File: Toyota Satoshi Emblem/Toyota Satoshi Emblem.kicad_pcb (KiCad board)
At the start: 2 copper layers, 175 x 100 mm, 337 parts

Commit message: v1.7
More changes to LED pcb. Realized I could link ambers in 3 link series and removing 6 resistors per letter (less heat). Have to redo everything again
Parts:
- removed the R2 at (70.2, 68.6)
- added REF**: Pad 1, afootprints:Pad 1, F.Cu at (81.6, 60.0)
- added REF**: Pad 1, afootprints:Pad 1, F.Cu at (73.7, 60.0)
- added REF**: Pad 1, afootprints:Pad 1, F.Cu at (89.5, 87.8)
- added REF**: Pad 1, afootprints:Pad 1, F.Cu at (97.5, 87.8)
- added REF**: Pad 1, afootprints:Pad 1, F.Cu at (77.6, 60.0)
- added REF**: Pad 1, afootprints:Pad 1, F.Cu at (93.5, 87.8)
- moved R36 187.8 mm to (99.8, 83.2), turned to 180 degrees
- moved R25 184.5 mm to (108.5, 92.8)
- moved R30 179.0 mm to (105.2, 86.0), turned to 180 degrees
- moved R27 176.3 mm to (100.2, 134.2), turned to 180 degrees
- moved R19 172.0 mm to (111.0, 99.0)
- moved R32 170.7 mm to (117.8, 114.2)
- moved D138 168.9 mm to (99.1, 316.7)
- moved R26 165.2 mm to (113.3, 114.2)
- moved R35 164.5 mm to (76.2, 100.4), turned to -90 degrees
- moved D25 164.4 mm to (107.8, 90.0)
- moved R33 162.4 mm to (96.5, 134.1), turned to 90 degrees
- moved R22 160.7 mm to (71.0, 120.5), turned to 90 degrees
- moved R23 152.6 mm to (80.5, 94.2), turned to 180 degrees
- moved R31 141.4 mm to (113.2, 92.5)
- moved R20 138.6 mm to (116.5, 120.8), turned to 180 degrees
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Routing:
- net Net-(D43-Pad1): track 0.00 -> 210.7 mm
- net Net-(J2-Pad2): track 0.00 -> 189.9 mm
- net Net-(D25-Pad1): track 0.00 -> 141.8 mm
- net Net-(D1-Pad1): track 151.3 -> 215.5 mm
- net Net-(D28-Pad2): track 0.00 -> 34.2 mm
- net Net-(D42-Pad1): track 0.00 -> 29.1 mm
- net Net-(D41-Pad1): track 0.00 -> 19.1 mm
- net Net-(D26-Pad2): track 0.00 -> 18.2 mm
- net Net-(D27-Pad2): track 0.00 -> 16.3 mm
- net Net-(D25-Pad2): track 0.00 -> 16.1 mm
- net Net-(D39-Pad1): track 0.00 -> 15.7 mm
- net Net-(D40-Pad1): track 0.00 -> 15.1 mm
- net Net-(R28-Pad2): track 0.00 -> 13.8 mm
- net Net-(D37-Pad1): track 0.00 -> 13.6 mm
- net Net-(D29-Pad2): track 0.00 -> 12.8 mm
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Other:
- outline, holes or cut-outs redrawn
- board text added: "7V"
- board text added: "amber"
- board text added: "dhoefer"
- board text added: "white"

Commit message: v1.8
Letter T is now complete
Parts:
- removed D100, D101, D102, D103, D104, D105, D106, D107, D108, D121, D122, D123, D124, D125, D126, D127, D128, D129, D130, D131, D132, D145, D146, D147, D148, D149, D150, D151, D152, D153, D154, D155, D156, D157, D158, D159, D160, D161, D162, D163, D164, D165, D166, D167, D168, D31, D32, D33, D34, D35, D36, D49, D50, D51, D52, D53, D54, D55, D56, D57, D58, D59, D60, D73, D74, D75, D76, D77, D78, D79, D80, D81, D82, D83, D84, D97, D98, D99: W_LED, afootprints:5730 LED W
- removed D109, D110, D111, D112, D113, D114, D115, D116, D117, D118, D119, D120, D133, D134, D135, D136, D137, D138, D139, D140, D141, D142, D143, D144, D169, D170, D171, D172, D173, D174, D175, D176, D177, D178, D179, D180, D181, D182, D183, D184, D185, D186, D187, D188, D189, D190, D191, D192, D37, D38, D39, D40, D41, D42, D43, D44, D45, D46, D47, D48, D61, D62, D63, D64, D65, D66, D67, D68, D69, D70, D71, D72, D85, D86, D87, D88, D89, D90, D91, D92, D93, D94, D95, D96: A_LED, afootprints:5730 LED A
- removed R100, R101, R102, R103, R104, R105, R106, R107, R108, R121, R122, R123, R124, R125, R126, R127, R128, R129, R13, R130, R131, R132, R133, R134, R135, R136, R137, R138, R139, R14, R140, R141, R142, R143, R144, R15, R16, R17, R18, R25, R26, R27, R28, R29, R30, R31, R32, R33, R34, R35, R36, R43, R44, R45, R46, R47, R48, R49, R50, R51, R52, R53, R54, R61, R62, R63, R64, R65, R66, R67, R68, R69, R70, R71, R72, R79, R80, R81, R82, R83, R84, R85, R86, R87, R88, R89, R90, R97, R98, R99: 8.2, afootprints:1206 R
- removed R109, R110, R111, R112, R113, R114, R115, R116, R117, R118, R119, R120, R19, R20, R21, R22, R23, R24, R37, R38, R39, R40, R41, R42, R55, R56, R57, R58, R59, R60, R73, R74, R75, R76, R77, R78, R91, R92, R93, R94, R95, R96: 3.3, afootprints:1206 R
- removed the REF** at (89.5, 87.8)
- removed the REF** at (97.5, 87.8)
- removed the REF** at (93.5, 87.8)
- D1, D10, D11, D12, D2, D3, D4, D5, D6, D7, D8, D9: value W_LED -> WLED
- D13, D14, D15, D16, D17, D18, D19, D20, D21, D22, D23, D24: value A_LED -> ALED
- D25, D26, D27, D28, D29, D30: value W_LED -> ALED; footprint afootprints:5730 LED W -> afootprints:5730 LED A
- R1, R2, R4, R5, R6: value 3.3 -> 4.7
- R10, R11, R12, R7, R8, R9: value 8.2 -> 4.7
- R3: value 3.3 -> 4,7
- moved D28 70.0 mm to (102.4, 62.5), turned to -90 degrees
- moved D27 66.7 mm to (89.8, 64.9)
- moved D29 53.9 mm to (89.8, 55.1), turned to 0 degrees
- moved D26 52.4 mm to (97.1, 61.8)
- moved D24 45.8 mm to (56.2, 69.0), turned to -90 degrees
- moved D25 33.2 mm to (97.1, 58.6), turned to 180 degrees
- moved D5 32.7 mm to (67.6, 55.4)
- moved D6 32.6 mm to (60.8, 48.4), turned to 90 degrees
- moved D9 31.9 mm to (82.4, 55.4)
- moved D30 31.4 mm to (75.0, 55.4), turned to 0 degrees
- moved D10 31.2 mm to (97.5, 55.5)
- moved D23 31.1 mm to (60.0, 64.6), turned to 90 degrees
- moved D17 30.9 mm to (52.8, 44.0), turned to 90 degrees
- moved D18 28.2 mm to (54.8, 56.6)
- moved D12 26.5 mm to (97.1, 64.9), turned to 0 degrees
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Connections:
- D11 pad 1: Net-(D11-Pad1) -> Net-(D1-Pad1)
- D12 pad 1: Net-(D12-Pad1) -> Net-(D11-Pad2)
- D14 pad 2: Net-(D14-Pad2) -> Net-(D13-Pad1)
- D15 pad 2: Net-(D15-Pad2) -> Net-(D14-Pad1)
- D17 pad 2: Net-(D17-Pad2) -> Net-(D16-Pad1)
- D18 pad 1: Net-(D18-Pad1) -> Net-(D15-Pad1)
- D18 pad 2: Net-(D18-Pad2) -> Net-(D17-Pad1)
- D19 pad 2: Net-(D13-Pad1) -> Net-(D19-Pad2)
- D2 pad 1: Net-(D1-Pad1) -> Net-(D1-Pad2)
- D20 pad 1: Net-(D19-Pad1) -> Net-(D20-Pad1)
- D20 pad 2: Net-(D14-Pad1) -> Net-(D19-Pad1)
- D21 pad 1: Net-(D19-Pad1) -> Net-(D15-Pad1)
- D21 pad 2: Net-(D15-Pad1) -> Net-(D20-Pad1)
- D22 pad 1: Net-(D19-Pad1) -> Net-(D22-Pad1)
- D22 pad 2: Net-(D16-Pad1) -> Net-(D22-Pad2)
- D23 pad 1: Net-(D19-Pad1) -> Net-(D23-Pad1)
- D23 pad 2: Net-(D17-Pad1) -> Net-(D22-Pad1)
- D24 pad 1: Net-(D19-Pad1) -> Net-(D15-Pad1)
- D24 pad 2: Net-(D18-Pad1) -> Net-(D23-Pad1)
- D26 pad 1: Net-(D25-Pad1) -> Net-(D26-Pad1)
- D26 pad 2: Net-(D26-Pad2) -> Net-(D25-Pad1)
- D27 pad 1: Net-(D25-Pad1) -> Net-(D15-Pad1)
- D27 pad 2: Net-(D27-Pad2) -> Net-(D26-Pad1)
- D28 pad 1: Net-(D25-Pad1) -> Net-(D28-Pad1)
- D29 pad 1: Net-(D25-Pad1) -> Net-(D29-Pad1)
- D29 pad 2: Net-(D29-Pad2) -> Net-(D28-Pad1)
- D30 pad 1: Net-(D25-Pad1) -> Net-(D15-Pad1)
- D30 pad 2: Net-(D30-Pad2) -> Net-(D29-Pad1)
- D4 pad 1: Net-(D1-Pad1) -> Net-(D3-Pad2)
- D4 pad 2: Net-(D10-Pad1) -> Net-(D4-Pad2)
- D5 pad 2: Net-(D11-Pad1) -> Net-(D5-Pad2)
- D6 pad 1: Net-(D1-Pad1) -> Net-(D5-Pad2)
- D6 pad 2: Net-(D12-Pad1) -> Net-(D6-Pad2)
- D7 pad 1: Net-(D1-Pad2) -> Net-(D1-Pad1)
- D8 pad 1: Net-(D2-Pad2) -> Net-(D7-Pad2)
- D9 pad 1: Net-(D3-Pad2) -> Net-(D1-Pad1)
- D9 pad 2: Net-(D9-Pad2) -> Net-(D10-Pad1)
- R1 pad 2: Net-(D7-Pad2) -> Net-(D2-Pad2)
- R10 pad 2: Net-(R10-Pad2) -> Net-(D22-Pad2)
- R11 pad 2: Net-(R11-Pad2) -> Net-(D25-Pad2)
- R12 pad 2: Net-(R12-Pad2) -> Net-(D28-Pad2)
- R2 pad 2: Net-(D8-Pad2) -> Net-(D4-Pad2)
- R3 pad 2: Net-(D9-Pad2) -> Net-(D6-Pad2)
- R4 pad 2: Net-(D10-Pad2) -> Net-(D8-Pad2)
- R5 pad 2: Net-(D11-Pad2) -> Net-(D10-Pad2)
- R7 pad 2: Net-(R13-Pad1) -> Net-(D13-Pad2)
- R8 pad 2: Net-(R14-Pad1) -> Net-(D16-Pad2)
- R9 pad 2: Net-(R15-Pad1) -> Net-(D19-Pad2)
- REF** pad 1: Net-(D19-Pad1) -> Net-(D15-Pad1)
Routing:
- net Net-(D43-Pad1): track 210.7 -> 0.00 mm
- net Net-(J2-Pad2): track 189.9 -> 0.00 mm
- net Net-(D25-Pad1): track 141.8 -> 3.20 mm
- net Net-(D1-Pad1): track 215.5 -> 81.7 mm
- net Net-(D19-Pad1): track 139.0 -> 8.05 mm
- net Net-(D15-Pad1): track 11.3 -> 71.8 mm
- net Net-(D17-Pad2): track 31.9 -> 0.00 mm
- net Net-(D42-Pad1): track 29.1 -> 0.00 mm
- net Net-(D28-Pad2): track 34.2 -> 13.0 mm
- net Net-(D12-Pad2): track 31.6 -> 12.4 mm
- net Net-(D41-Pad1): track 19.1 -> 0.00 mm
- net Net-(D12-Pad1): track 19.0 -> 0.00 mm
- net Net-(D26-Pad2): track 18.2 -> 0.00 mm
- net Net-(D28-Pad1): track 0.00 -> 17.4 mm
- net Net-(D27-Pad2): track 16.3 -> 0.00 mm
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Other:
- board text added: "7.5V"
- board text added: "Daniel Hoefer"
- board text added: "Isaiah 60:1"
- board text added: "a"
- board text added: "w"
- board text removed: "7V"
- board text removed: "amber"
- board text removed: "dhoefer"
- board text removed: "white"

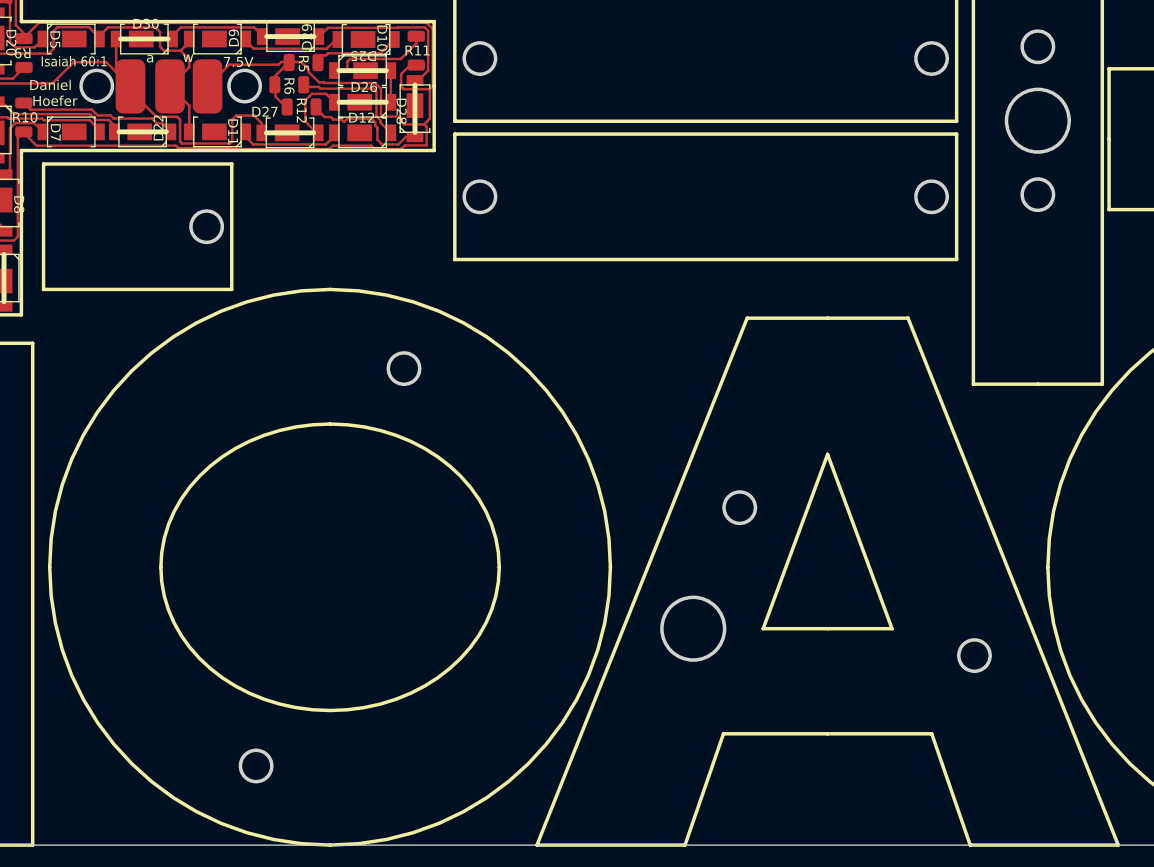
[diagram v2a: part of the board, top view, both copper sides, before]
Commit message: v1.9
Letter O and A are now complete
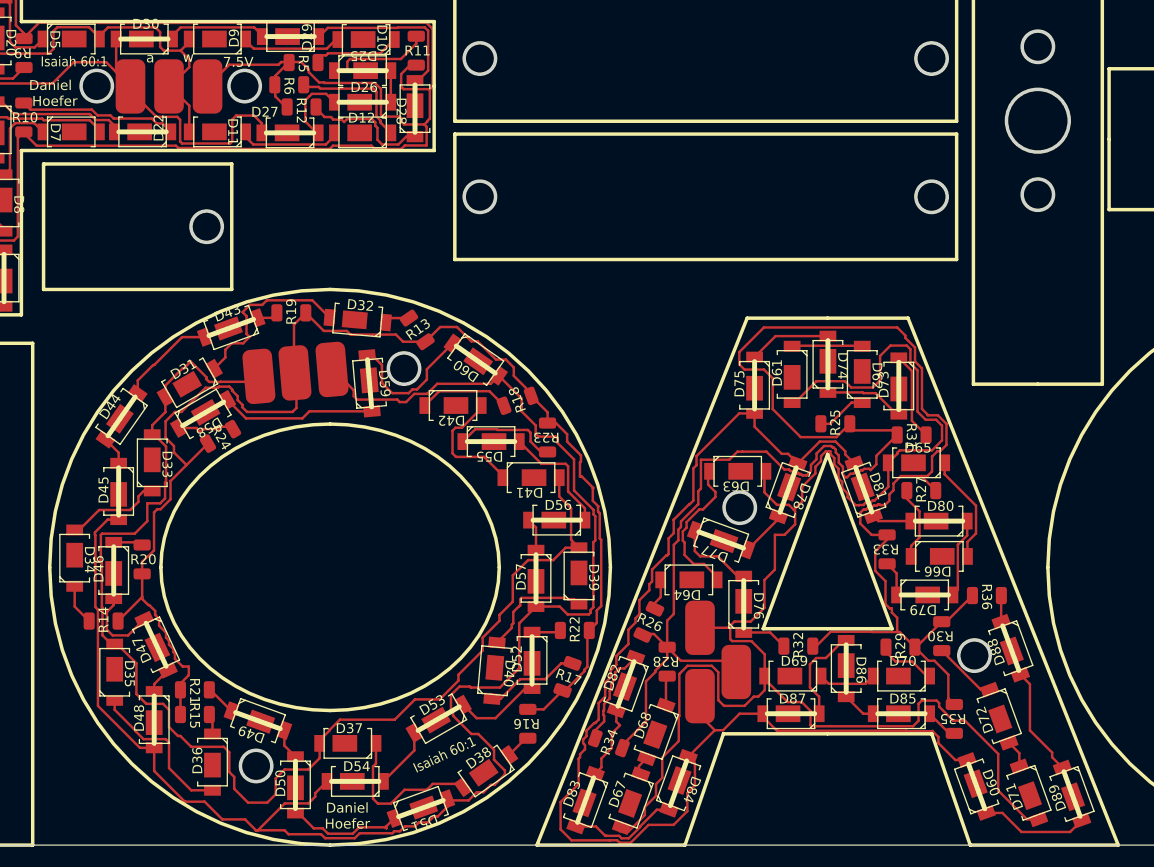
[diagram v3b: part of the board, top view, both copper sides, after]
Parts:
- added D31: WLED, afootprints:5730 LED W, F.Cu at (79.6, 90.2)
- added D32: WLED, afootprints:5730 LED W, F.Cu at (96.6, 83.8)
- added D33: WLED, afootprints:5730 LED W, F.Cu at (75.8, 98.3)
- added D34: WLED, afootprints:5730 LED W, F.Cu at (68.0, 108.0)
- added D35: WLED, afootprints:5730 LED W, F.Cu at (72.0, 119.5)
- added D36: WLED, afootprints:5730 LED W, F.Cu at (81.9, 128.6)
- added D37: WLED, afootprints:5730 LED W, F.Cu at (95.6, 126.7)
- added D38: WLED, afootprints:5730 LED W, F.Cu at (109.6, 129.5)
- added D39: WLED, afootprints:5730 LED W, F.Cu at (119.0, 109.8)
- added D40: WLED, afootprints:5730 LED W, F.Cu at (110.5, 119.3)
- added D41: WLED, afootprints:5730 LED W, F.Cu at (114.2, 99.8)
- added D42: WLED, afootprints:5730 LED W, F.Cu at (106.2, 92.5)
- added D43: ALED, afootprints:5730 LED A, F.Cu at (83.8, 84.6)
- added D44: ALED, afootprints:5730 LED A, F.Cu at (72.7, 93.6)
- added D45: ALED, afootprints:5730 LED A, F.Cu at (72.4, 101.2)
- added D46: ALED, afootprints:5730 LED A, F.Cu at (71.9, 109.2)
- added D47: ALED, afootprints:5730 LED A, F.Cu at (76.2, 116.7)
- added D48: ALED, afootprints:5730 LED A, F.Cu at (76.0, 124.3)
- added D49: ALED, afootprints:5730 LED A, F.Cu at (86.5, 124.4)
- added D50: ALED, afootprints:5730 LED A, F.Cu at (90.3, 130.9)
- added D51: ALED, afootprints:5730 LED A, F.Cu at (103.0, 133.3)
- added D52: ALED, afootprints:5730 LED A, F.Cu at (114.2, 118.3)
- added D53: ALED, afootprints:5730 LED A, F.Cu at (104.8, 124.2)
- added D54: ALED, afootprints:5730 LED A, F.Cu at (96.3, 130.6)
- added D55: ALED, afootprints:5730 LED A, F.Cu at (110.1, 96.2)
- added D56: ALED, afootprints:5730 LED A, F.Cu at (116.8, 104.1)
- added D57: ALED, afootprints:5730 LED A, F.Cu at (114.7, 110.0)
- added D58: ALED, afootprints:5730 LED A, F.Cu at (81.0, 93.3)
- added D59: ALED, afootprints:5730 LED A, F.Cu at (97.8, 90.2)
- added D60: ALED, afootprints:5730 LED A, F.Cu at (108.5, 87.8)
- added D61: WLED, afootprints:5730 LED W, F.Cu at (140.6, 89.3)
- added D62: WLED, afootprints:5730 LED W, F.Cu at (147.7, 89.3)
- added D63: WLED, afootprints:5730 LED W, F.Cu at (135.1, 99.2)
- added D64: WLED, afootprints:5730 LED W, F.Cu at (130.1, 110.2)
- added D65: WLED, afootprints:5730 LED W, F.Cu at (153.2, 98.3)
- added D66: WLED, afootprints:5730 LED W, F.Cu at (155.5, 107.8)
- added D67: WLED, afootprints:5730 LED W, F.Cu at (124.3, 132.5)
- added D68: WLED, afootprints:5730 LED W, F.Cu at (126.8, 125.5)
- added D69: WLED, afootprints:5730 LED W, F.Cu at (140.7, 119.9)
- added D70: WLED, afootprints:5730 LED W, F.Cu at (151.6, 119.9)
- added D71: WLED, afootprints:5730 LED W, F.Cu at (164.6, 131.7)
- added D72: WLED, afootprints:5730 LED W, F.Cu at (161.5, 124.0)
- added D73: ALED, afootprints:5730 LED A, F.Cu at (151.4, 90.5)
- added D74: ALED, afootprints:5730 LED A, F.Cu at (144.2, 88.3)
- added D75: ALED, afootprints:5730 LED A, F.Cu at (136.8, 90.5)
- added D76: ALED, afootprints:5730 LED A, F.Cu at (135.7, 112.6)
- added D77: ALED, afootprints:5730 LED A, F.Cu at (133.4, 106.1)
- added D78: ALED, afootprints:5730 LED A, F.Cu at (140.2, 101.0)
- added D79: ALED, afootprints:5730 LED A, F.Cu at (154.0, 111.7)
- added D80: ALED, afootprints:5730 LED A, F.Cu at (155.4, 104.2)
- added D81: ALED, afootprints:5730 LED A, F.Cu at (147.8, 101.0)
- added D82: ALED, afootprints:5730 LED A, F.Cu at (123.8, 120.7)
- added D83: ALED, afootprints:5730 LED A, F.Cu at (119.7, 132.4)
- added D84: ALED, afootprints:5730 LED A, F.Cu at (129.1, 130.7)
- added D85: ALED, afootprints:5730 LED A, F.Cu at (151.6, 123.7)
- added D86: ALED, afootprints:5730 LED A, F.Cu at (146.1, 119.1)
- added D87: ALED, afootprints:5730 LED A, F.Cu at (140.5, 123.7)
- added D88: ALED, afootprints:5730 LED A, F.Cu at (162.7, 117.1)
- added D89: ALED, afootprints:5730 LED A, F.Cu at (168.9, 131.8)
- added D90: ALED, afootprints:5730 LED A, F.Cu at (159.3, 131.1)
- added R13: 4.7, afootprints:1206 R, F.Cu at (102.7, 84.8)
- added R14: 4.7, afootprints:1206 R, F.Cu at (70.9, 114.3)
- added R15: 4,7, afootprints:1206 R, F.Cu at (80.1, 123.8)
- added R16: 4.7, afootprints:1206 R, F.Cu at (113.8, 124.7)
- added R17: 4.7, afootprints:1206 R, F.Cu at (117.8, 120.0)
- added R18: 4.7, afootprints:1206 R, F.Cu at (112.8, 92.0)
- added R19: 4.7, afootprints:1206 R, F.Cu at (89.9, 83.1)
- added R20: 4.7, afootprints:1206 R, F.Cu at (74.8, 108.1)
- added R21: 4.7, afootprints:1206 R, F.Cu at (80.1, 121.3)
- added R22: 4.7, afootprints:1206 R, F.Cu at (118.6, 115.2)
- added R23: 4.7, afootprints:1206 R, F.Cu at (115.8, 95.7)
- added R24: 4.7, afootprints:1206 R, F.Cu at (82.7, 95.7)
- added R25: 4.7, afootprints:1206 R, F.Cu at (145.0, 94.3)
- added R26: 4.7, afootprints:1206 R, F.Cu at (126.1, 114.4)
- added R27: 4,7, afootprints:1206 R, F.Cu at (153.7, 101.1)
- added R28: 4.7, afootprints:1206 R, F.Cu at (127.9, 118.4)
- added R29: 4.7, afootprints:1206 R, F.Cu at (151.6, 116.9)
- added R30: 4.7, afootprints:1206 R, F.Cu at (155.7, 115.8)
- added R31: 4.7, afootprints:1206 R, F.Cu at (152.7, 95.5)
- added R32: 4.7, afootprints:1206 R, F.Cu at (141.2, 116.8)
- added R33: 4.7, afootprints:1206 R, F.Cu at (150.2, 107.0)
- added R34: 4.7, afootprints:1206 R, F.Cu at (122.0, 126.7)
- added R35: 4.7, afootprints:1206 R, F.Cu at (157.0, 124.2)
- added R36: 4.7, afootprints:1206 R, F.Cu at (160.3, 111.8)
- added REF**: Pad 1, afootprints:Pad 1, F.Cu at (131.2, 115.0)
- added REF**: Pad 1, afootprints:Pad 1, F.Cu at (90.2, 89.2)
- added REF**: Pad 1, afootprints:Pad 1, F.Cu at (86.6, 89.5)
- added REF**: Pad 1, afootprints:Pad 1, F.Cu at (131.2, 121.9)
- added REF**: Pad 1, afootprints:Pad 1, F.Cu at (94.0, 88.8)
- added REF**: Pad 1, afootprints:Pad 1, F.Cu at (134.9, 119.5)
- moved REF** 0.10 mm to (77.5, 60.2)
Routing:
- net Net-(R25-Pad1): track 0.00 -> 185.0 mm
- net Net-(D45-Pad1): track 0.00 -> 162.1 mm
- net Net-(D61-Pad1): track 0.00 -> 161.4 mm
- net Net-(J2-Pad2): track 0.00 -> 136.3 mm
- net Net-(D31-Pad1): track 0.00 -> 127.1 mm
- net Net-(D75-Pad1): track 0.00 -> 124.4 mm
- net Net-(D31-Pad2): track 0.00 -> 18.2 mm
- net Net-(D37-Pad2): track 0.00 -> 16.0 mm
- net Net-(D35-Pad2): track 0.00 -> 15.8 mm
- net Net-(D58-Pad1): track 0.00 -> 15.7 mm
- net Net-(D63-Pad2): track 0.00 -> 15.1 mm
- net Net-(D59-Pad1): track 0.00 -> 14.0 mm
- net Net-(D41-Pad2): track 0.00 -> 12.7 mm
- net Net-(D55-Pad1): track 0.00 -> 12.1 mm
- net Net-(D50-Pad1): track 0.00 -> 11.8 mm
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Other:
- outline, holes or cut-outs redrawn
